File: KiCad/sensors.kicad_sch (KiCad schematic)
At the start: 12 parts, among them U6 LTR-303ALS-01, U8 GXHTC3

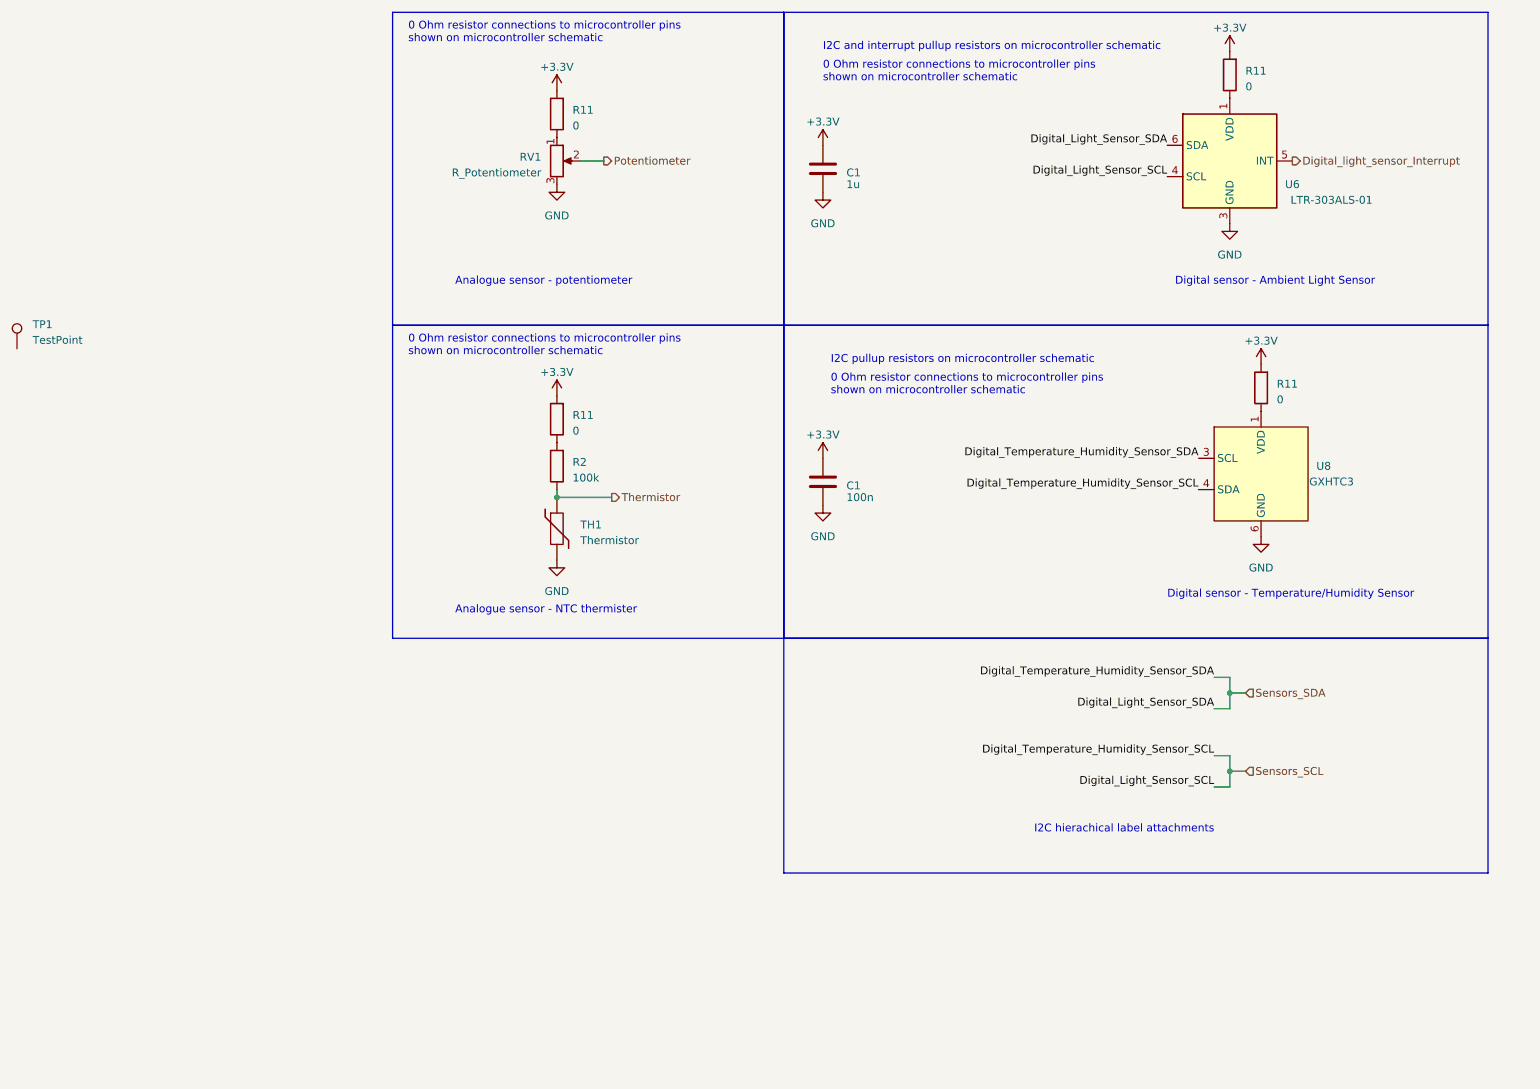
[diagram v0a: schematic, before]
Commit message: sensors schematic changes, net label name changes
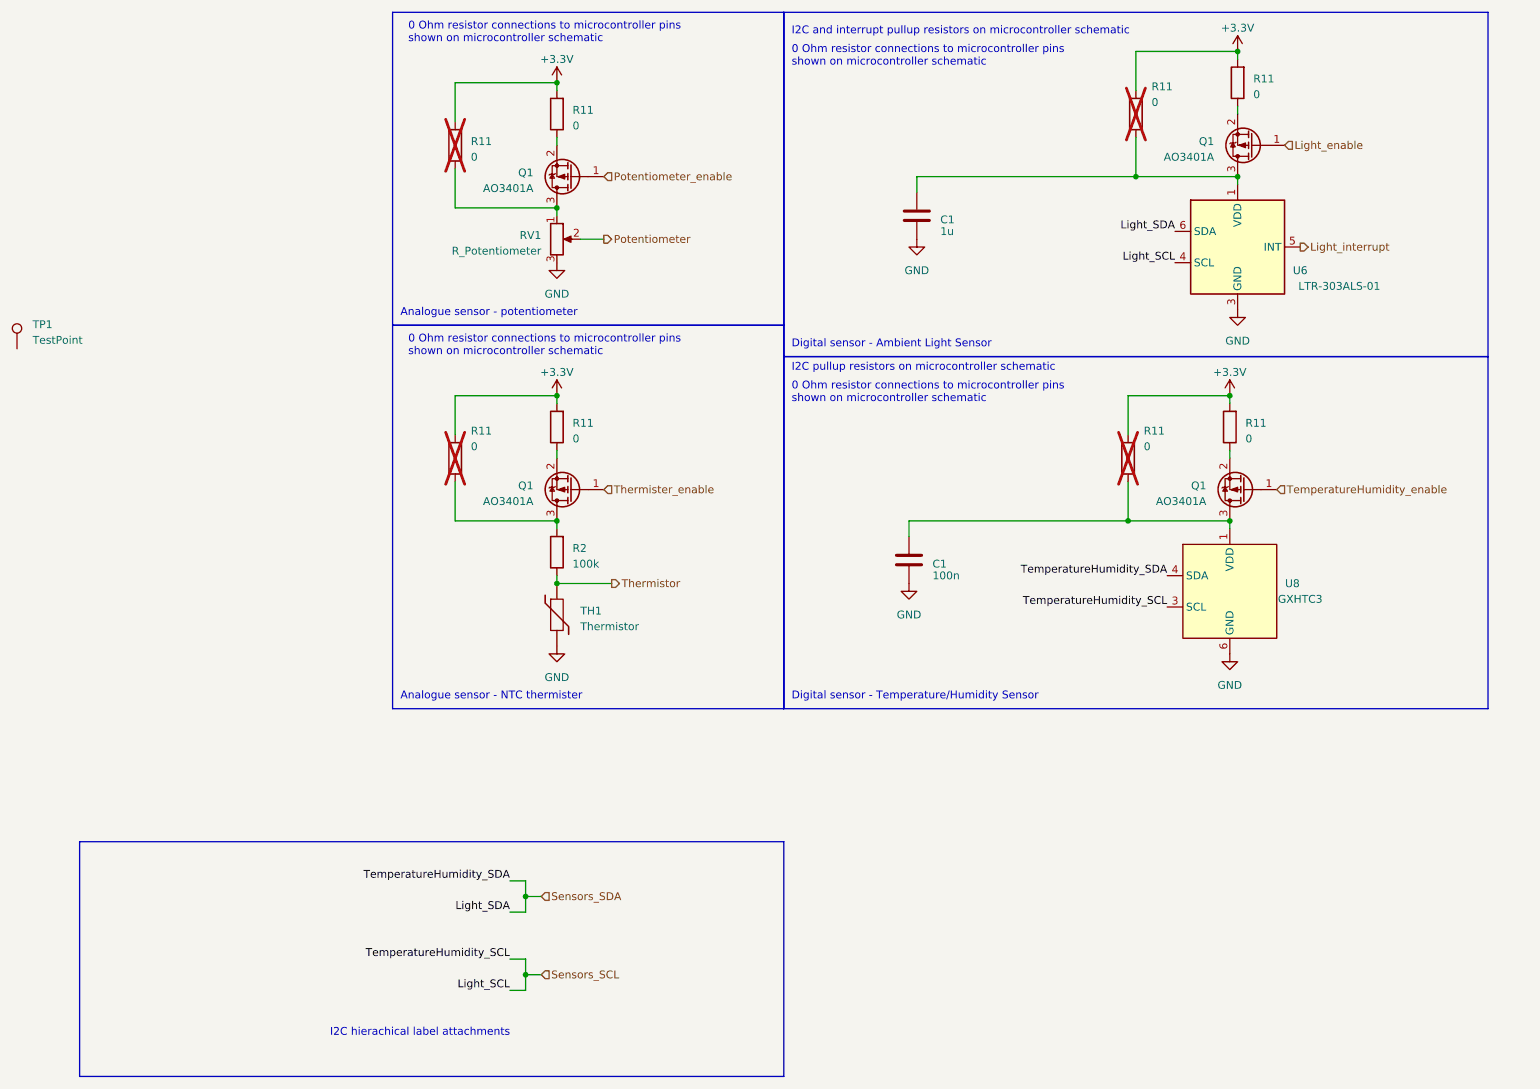
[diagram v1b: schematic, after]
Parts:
- removed R11 (x3): 0, symbol Device:R
- added Q1 (x4): AO3401A, Package_TO_SOT_SMD:SOT-23, symbol Transistor_FET:AO3401A
- added R11 (x7): 0, symbol Device:R
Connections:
- net +3.3V: now also R11.2, R11.2, R11.2, R11.2, R11.2, R11.2, R11.2; no longer C1.1, C1.1
- net Sensors_SCL: now also U8.3 (SCL); no longer U8.4 (SDA)
- net Sensors_SDA: now also U8.4 (SDA); no longer U8.3 (SCL)
- net at R2.2: now also Q1.3 (D), R11.1
- net at RV1.1: now also Q1.3 (D), R11.1; no longer R11.1
- net at U6.1 (VDD): now also C1.1, Q1.3 (D), R11.1
- net at U8.1 (VDD): now also C1.1, Q1.3 (D), R11.1
- net Digital_light_sensor_Interrupt renamed Light_interrupt
- new net: Q1.2 (S), R11.1 (x4)
- new net Light_enable: Q1.1 (G)
- new net Potentiometer_enable: Q1.1 (G)
- new net TemperatureHumidity_enable: Q1.1 (G)
- new net Thermister_enable: Q1.1 (G)
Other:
- moved on the sheet: C1, R2, RV1, TH1, U6, U8

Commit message: added test points to sensor schem
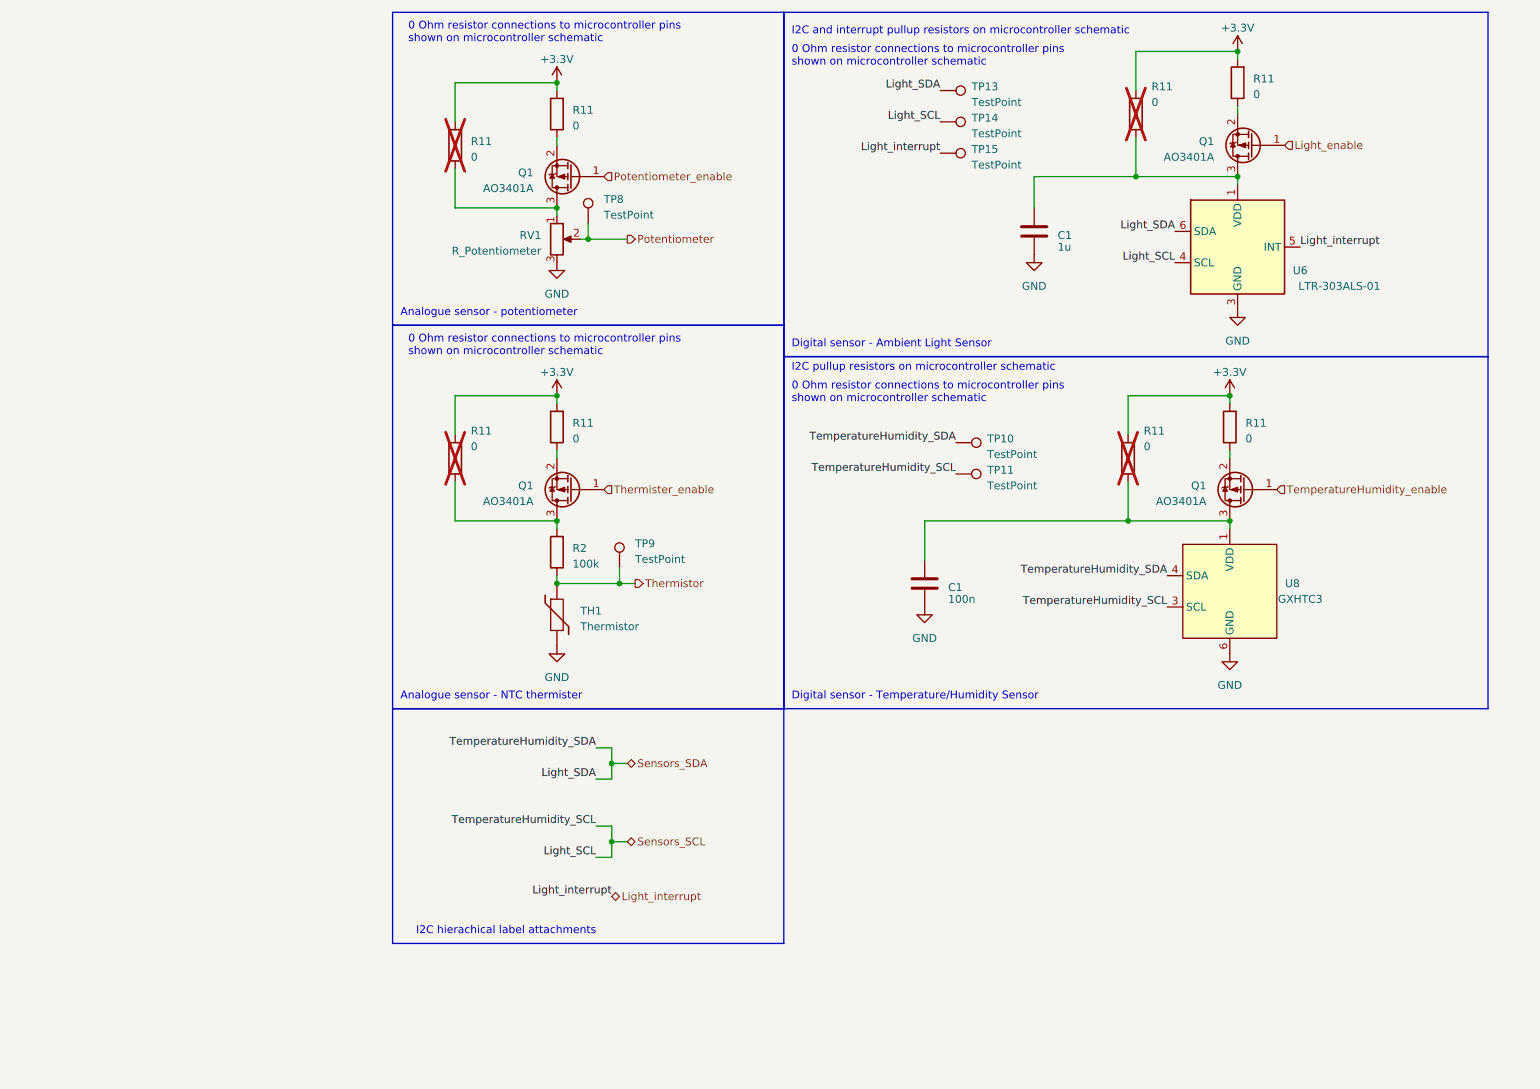
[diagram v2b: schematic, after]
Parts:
- removed TP1: TestPoint, symbol Connector:TestPoint
- added TP10, TP11, TP13, TP14, TP15, TP8, TP9: TestPoint, symbol Connector:TestPoint
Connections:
- net Light_interrupt: now also TP15.1
- net Potentiometer: now also TP8.1
- net Sensors_SCL: now also TP11.1, TP14.1
- net Sensors_SDA: now also TP10.1, TP13.1
- net Thermistor: now also TP9.1
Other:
- moved on the sheet: C1

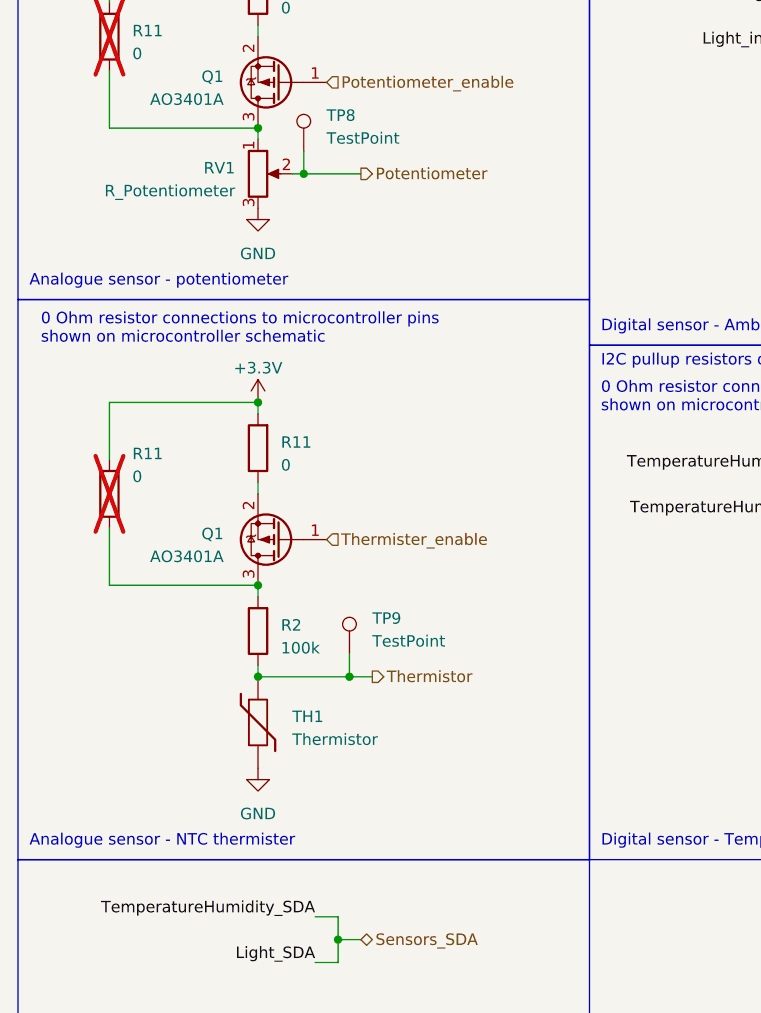
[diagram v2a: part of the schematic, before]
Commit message: changed a bunch of net labels, changed some uc schem stuff
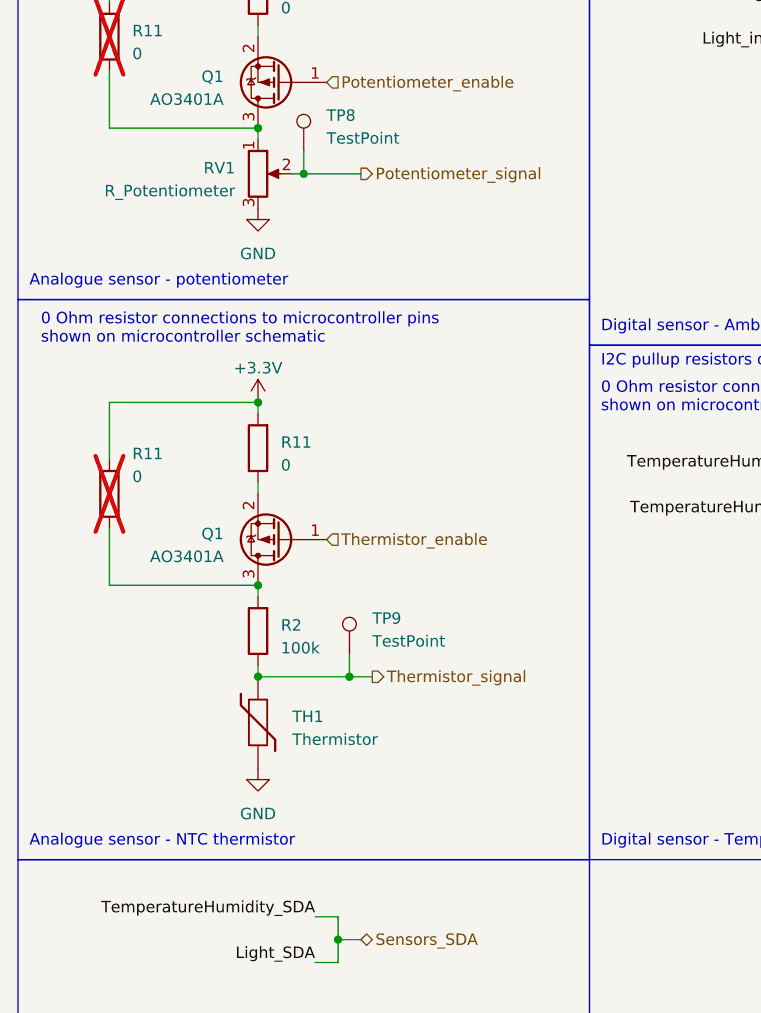
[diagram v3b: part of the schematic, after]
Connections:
- net Potentiometer renamed Potentiometer_signal
- net Thermister_enable renamed Thermistor_enable
- net Thermistor renamed Thermistor_signal
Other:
- note added: "Analogue sensor - NTC thermistor"
- note removed: "Analogue sensor - NTC thermister"
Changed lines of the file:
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@@
     (effects (font (size 1.27 1.27)) (justify left bottom))
   )
-  (text "Analogue sensor - NTC thermister" (at 99.06 129.54 0)
+  (text "Analogue sensor - NTC thermistor" (at 99.06 129.54 0)
     (effects (font (size 1.27 1.27)) (justify left bottom))
   )
@@
     (effects (font (size 1.27 1.27)) (justify left))
   )
-  (hierarchical_label "Thermistor" (shape output) (at 137.16 110.49 0) (fields_autoplaced)
+  (hierarchical_label "Thermistor_signal" (shape output) (at 137.16 110.49 0) (fields_autoplaced)
     (effects (font (size 1.27 1.27)) (justify left))
   )
-  (hierarchical_label "Potentiometer" (shape output) (at 135.89 54.61 0) (fields_autoplaced)
+  (hierarchical_label "Potentiometer_signal" (shape output) (at 135.89 54.61 0) (fields_autoplaced)
     (effects (font (size 1.27 1.27)) (justify left))
   )
@@
     (effects (font (size 1.27 1.27)) (justify left))
   )
-  (hierarchical_label "Thermister_enable" (shape input) (at 132.08 95.25 0) (fields_autoplaced)
+  (hierarchical_label "Thermistor_enable" (shape input) (at 132.08 95.25 0) (fields_autoplaced)
     (effects (font (size 1.27 1.27)) (justify left))
   )
